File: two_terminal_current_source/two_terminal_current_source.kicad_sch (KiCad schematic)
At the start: 19 parts, among them Q1 MMBT3904, Q2 MMBT3906, Q3 MMBT3904, U1 TL431DBZ, U2 LM358

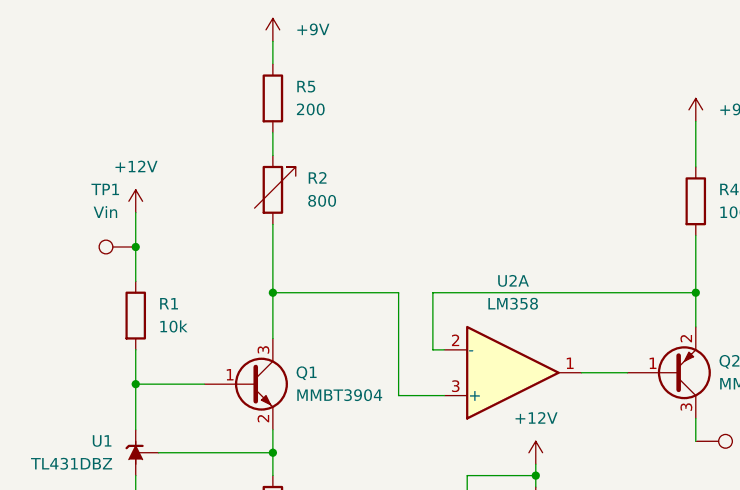
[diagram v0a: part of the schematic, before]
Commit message: Move connectors, fix silkscreen, add identifier
* Move output to left side to suit mechanical enclosure
* Move sense resistor input pads to side of board to suit mechanical enclosure
* Move more component identifiers to silkscreen layer
* Add board version, identification
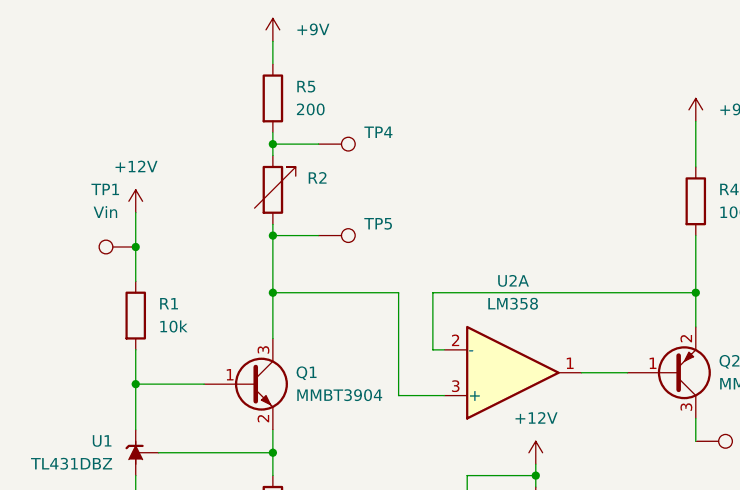
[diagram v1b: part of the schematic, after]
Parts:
- added TP4, TP5: (no value), Connector_PinHeader_2.54mm:PinHeader_1x01_P2.54mm_Vertical, symbol Connector:TestPoint
- R2: value 800 -> (none); footprint Connector_PinHeader_2.54mm:PinHeader_1x02_P2.54mm_Vertical -> (none)
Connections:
- net at Q1.3 (C), R2.2, U2.3 (+): now also TP5.1
- net at R2.1, R5.2: now also TP4.1
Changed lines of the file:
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@@
   (junction (at 185.42 62.23) (diameter 0) (color 0 0 0 0)
   )
+  (junction (at 63.5 43.18) (diameter 0) (color 0 0 0 0)
+  )
+  (junction (at 63.5 33.02) (diameter 0) (color 0 0 0 0)
+  )
   (junction (at 48.26 59.69) (diameter 0) (color 0 0 0 0)
   )
@@
     (stroke (width 0) (type default) (color 0 0 0 0))
   )
-  (wire (pts (xy 63.5 31.75) (xy 63.5 34.29))
+  (wire (pts (xy 63.5 31.75) (xy 63.5 33.02))
     (stroke (width 0) (type default) (color 0 0 0 0))
   )
@@
     (stroke (width 0) (type default) (color 0 0 0 0))
   )
-  (wire (pts (xy 63.5 41.91) (xy 63.5 49.53))
+  (wire (pts (xy 63.5 43.18) (xy 68.58 43.18))
+    (stroke (width 0) (type default) (color 0 0 0 0))
+  )
+  (wire (pts (xy 63.5 41.91) (xy 63.5 43.18))
     (stroke (width 0) (type default) (color 0 0 0 0))
   )
@@
     (stroke (width 0) (type default) (color 0 0 0 0))
   )
+  (wire (pts (xy 63.5 43.18) (xy 63.5 49.53))
+    (stroke (width 0) (type default) (color 0 0 0 0))
+  )
+  (wire (pts (xy 63.5 33.02) (xy 63.5 34.29))
+    (stroke (width 0) (type default) (color 0 0 0 0))
+  )
   (wire (pts (xy 63.5 67.31) (xy 63.5 69.85))
     (stroke (width 0) (type default) (color 0 0 0 0))
   )
   (wire (pts (xy 82.55 55.88) (xy 81.28 55.88))
+    (stroke (width 0) (type default) (color 0 0 0 0))
+  )
+  (wire (pts (xy 63.5 33.02) (xy 68.58 33.02))
     (stroke (width 0) (type default) (color 0 0 0 0))
   )
@@
     (pin "1")
   )
+  (symbol (lib_id "Connector:TestPoint") (at 68.58 33.02 270) (unit 1)
+    (in_bom yes) (on_board yes) (fields_autoplaced)
+    (property "Reference" "TP4" (id 0) (at 73.66 31.7499 90)
+      (effects (font (size 1.27 1.27)) (justify left))
+    )
+    (property "Value" "" (id 1) (at 73.66 34.2899 90)
+      (effects (font (size 1.27 1.27)) (justify left))
+    )
+    (property "Footprint" "Connector_PinHeader_2.54mm:PinHeader_1x01_P2.54mm_Vertical" (id 2) (at 68.58 38.1 0)
+      (effects (font (size 1.27 1.27)) hide)
+    )
+    (property "Datasheet" "~" (id 3) (at 68.58 38.1 0)
+      (effects (font (size 1.27 1.27)) hide)
+    )
+    (pin "1")
+  )
   (symbol (lib_id "power:+12V") (at 144.78 33.02 0) (unit 1)
     (in_bom yes) (on_board yes) (fields_autoplaced)
@@
   )
   (symbol (lib_id "Device:R_Variable") (at 63.5 38.1 0) (unit 1)
-    (in_bom yes) (on_board yes) (fields_autoplaced)
+    (in_bom yes) (on_board no) (fields_autoplaced)
     (property "Reference" "R2" (id 0) (at 67.31 36.8299 0)
       (effects (font (size 1.27 1.27)) (justify left))
     )
-    (property "Value" "800" (id 1) (at 67.31 39.3699 0)
-      (effects (font (size 1.27 1.27)) (justify left))
-    )
-    (property "Footprint" "Connector_PinHeader_2.54mm:PinHeader_1x02_P2.54mm_Vertical" (id 2) (at 61.722 38.1 90)
+    (property "Value" "" (id 1) (at 67.31 39.3699 0)
+      (effects (font (size 1.27 1.27)) (justify left))
+    )
+    (property "Footprint" "" (id 2) (at 61.722 38.1 90)
       (effects (font (size 1.27 1.27)) hide)
     )
@@
     (pin "1")
     (pin "2")
+  )
+  (symbol (lib_id "Connector:TestPoint") (at 68.58 43.18 270) (unit 1)
+    (in_bom yes) (on_board yes) (fields_autoplaced)
+    (property "Reference" "TP5" (id 0) (at 73.66 41.9099 90)
+      (effects (font (size 1.27 1.27)) (justify left))
+    )
+    (property "Value" "" (id 1) (at 73.66 44.4499 90)
+      (effects (font (size 1.27 1.27)) (justify left))
+    )
+    (property "Footprint" "Connector_PinHeader_2.54mm:PinHeader_1x01_P2.54mm_Vertical" (id 2) (at 68.58 48.26 0)
+      (effects (font (size 1.27 1.27)) hide)
+    )
+    (property "Datasheet" "~" (id 3) (at 68.58 48.26 0)
+      (effects (font (size 1.27 1.27)) hide)
+    )
+    (pin "1")
   )
   (symbol (lib_id "Device:R") (at 144.78 55.88 0) (unit 1)
@@
       (reference "TP3") (unit 1) (value "GND") (footprint "Connector_PinHeader_2.54mm:PinHeader_1x01_P2.54mm_Vertical")
     )
+    (path "/8e3bf11d-27b2-400f-a5a8-f03f0fb26c1a"
+      (reference "TP4") (unit 1) (value "RsA") (footprint "Connector_PinHeader_2.54mm:PinHeader_1x01_P2.54mm_Vertical")
+    )
+    (path "/da62e9e6-8ee1-4ee2-ad70-32c2e1a62c66"
+      (reference "TP5") (unit 1) (value "RsB") (footprint "Connector_PinHeader_2.54mm:PinHeader_1x01_P2.54mm_Vertical")
+    )
     (path "/09b335de-46b0-4855-aa0b-ff39da113196"
